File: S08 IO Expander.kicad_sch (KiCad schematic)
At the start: 13 parts, among them Q23 BSS138, U11 PCAL9714

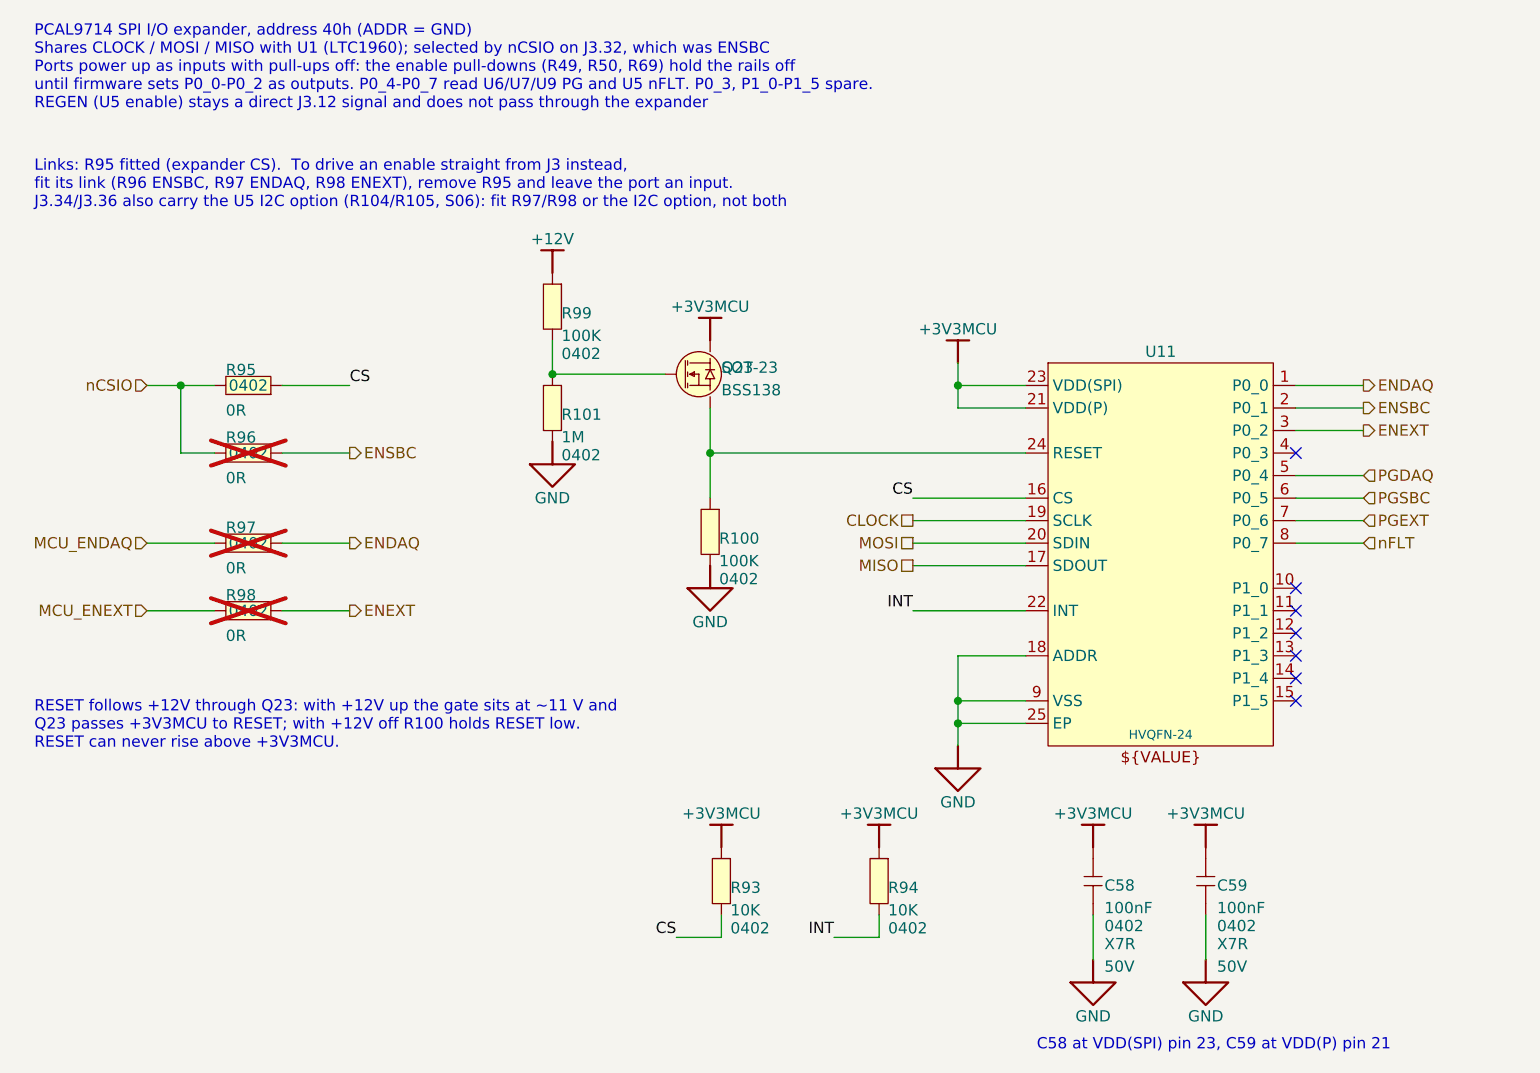
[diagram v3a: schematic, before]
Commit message: Final-revision value changes and standard R/C symbols
Values (schematic and PCB):
- C2 100uF -> 82uF, matching the ordered 35SVPF82M
- C46, C47, C51 (TPS22811 DVDT) 4.7nF -> 1.8nF CC0402KRX7R9BB182 for a
  shorter output ramp
- R24-R27 10R -> 0R; D9, D10 and R36 DNP
- R14 0.01R -> 0.012R PA2512FKF7W0R012E

Symbols:
- All 160 resistors and capacitors now use Device:R, Device:C and
  Device:C_Polarized; the 76 per-value R/C symbols are removed from the
  project library. Connectivity is unchanged (netlist compared).
- Value is now the displayed field instead of ALTIUM_VALUE, which had left
  R1, C39 and R54 showing their old values. ALTIUM_VALUE synced with Value
  on R1, C39, R54, D1, Q1, Q3 and L1.
- Net-(C40-+) is now Net-(U5-ISNSP); renamed on the PCB and in the
  PWR 15A net class pattern.

Co-Authored-By: Claude Opus 5.5 <noreply@anthropic.com>
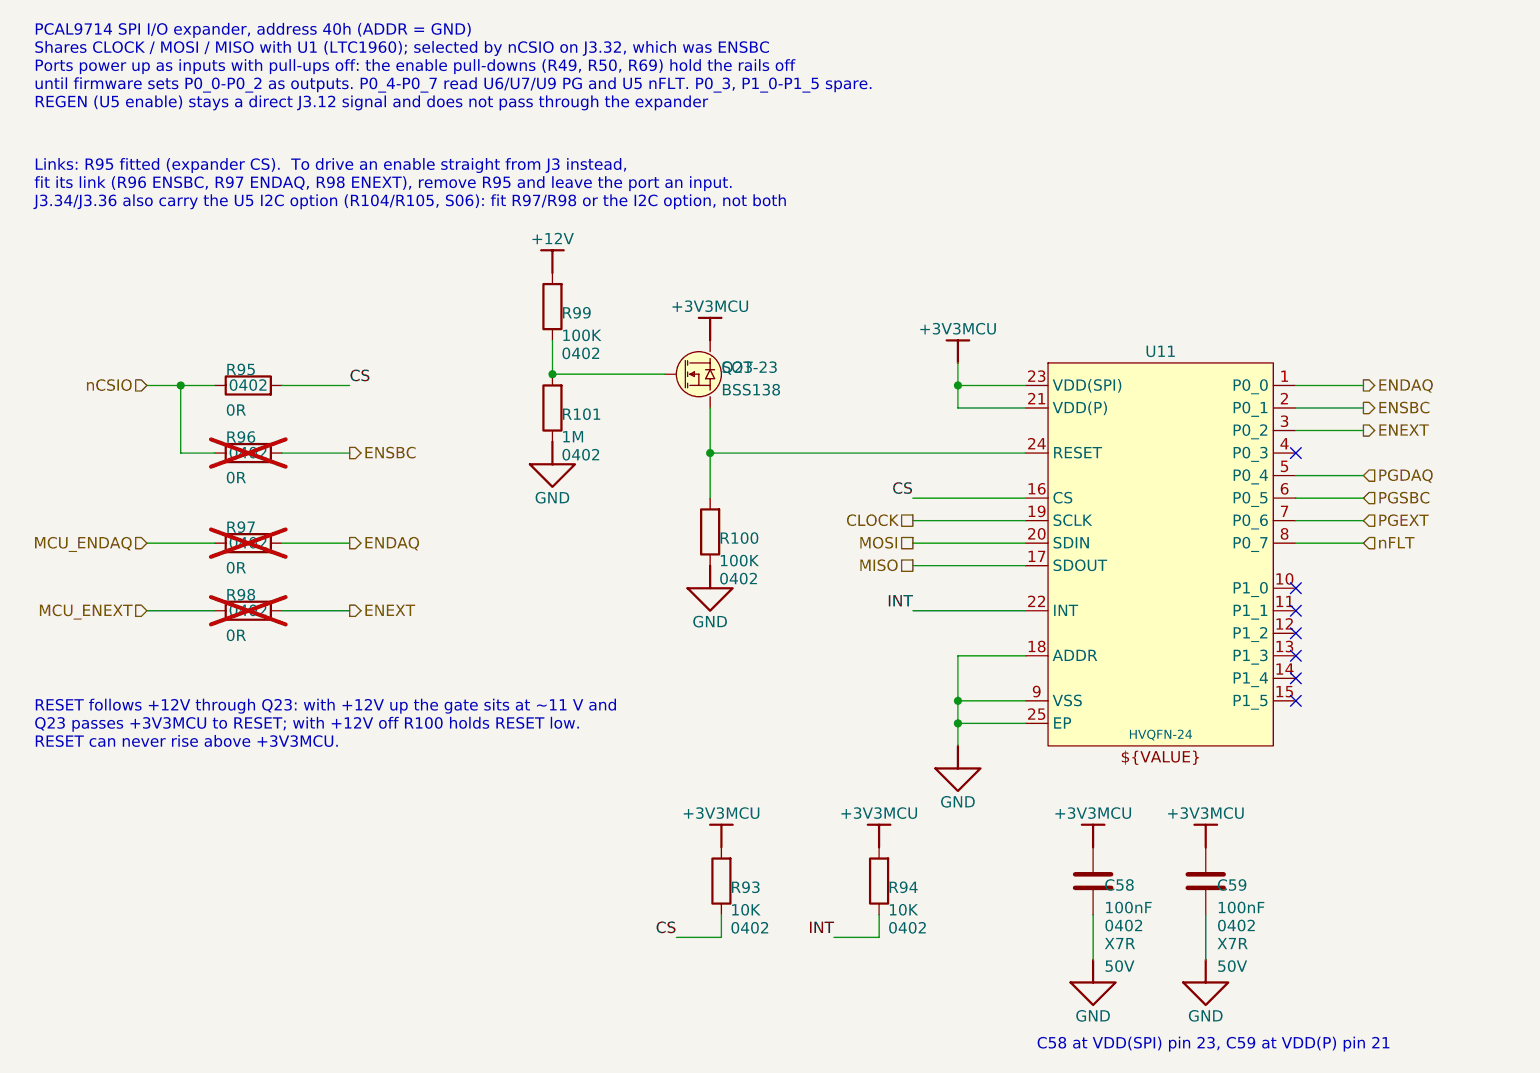
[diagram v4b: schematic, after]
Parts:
- C58, C59: symbol Lattech Systems:Capacitor 100nF 50V X7R 0402 -> Device:C
- R100, R99: symbol Lattech Systems:Resistor 100K 1% 0402 -> Device:R
- R101: symbol Lattech Systems:Resistor 1M 1% 0402 -> Device:R
- R93, R94: symbol Lattech Systems:Resistor 10K 1% 0402 -> Device:R
- R95, R96, R97, R98: symbol Lattech Systems:Resistor 0R 0402 -> Device:R

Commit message: Retune load-switch OVLO and PG dividers; add design constraint notes
- R90-R92 1M -> 1.07M: OVLO trips at 14.0 V (13.40-14.69 V) and recovers
  below 12.75 V (at least 12.23 V), so a tripped switch always comes back
  on the 12.03 V rail. R101 (Q23 gate divider) -> 1.07M to share the line.
- PGTH dividers R59/R61/R76 1M -> 100K and R60/R62/R77 130K -> 13K: same
  10.43 V threshold, but the +-1 uA pin leakage now moves it 0.1 V, not
  1 V; worst-case rising 10.93 V instead of 11.84 V.
- Schematic notes for the W16 constraints: J2 contacts (S01), R16 latching
  breaker and ED29/QE29 trip currents (S03), R19 vs L1 saturation (S04),
  R22 presence pull-up (S05), R42 and the U5 MODE/ILIMCOMP/VCC2 pins (S06),
  and the OVLO/PG divider settings (S07).
- README: OVLO and PG divider figures, and the EN_CONST_TDEAD default for
  the I2C build.

Co-Authored-By: Claude Opus 5.5 <noreply@anthropic.com>
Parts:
- R101: value 1M -> 1.07M; ALTIUM_VALUE 1M -> 1.07M
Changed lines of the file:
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@@
 			)
 		)
-		(property "Value" "1M"
+		(property "Value" "1.07M"
 			(at 122.936 111.76 0)
 			(show_name no)
@@
 			)
 		)
-		(property "Description" "Resistor 1M 1% 0402"
+		(property "Description" "Resistor 1.07M 1% 0402"
 			(at 121.92 109.22 90)
 			(hide yes)
@@
 			)
 		)
-		(property "ALTIUM_VALUE" "1M"
+		(property "ALTIUM_VALUE" "1.07M"
 			(at 120.904 104.902 0)
 			(hide yes)

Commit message: Add an 11 V undervoltage lockout to the DAQ load switch
- R108 100K from +12V over R49 (100K -> 12K) on U6 EN/UVLO: on at 11.2 V
  (10.77-11.69 V), off at 10.17 V (9.83-10.66 V). The TPS22811's fixed
  hysteresis makes 11 V the turn-on point.
- Q24 (BSS138) from EN/UVLO to GND takes over the enable. Its gate is biased
  from +12V by R109 100K / R110 27K (2.55 V), so U6 stays in shutdown when
  the expander is in reset, unpowered, or the MCU board is off.
- The expander net ENDAQ is now nENDAQ, active low (S07, S08, root sheet).
  The gate stays under 3.3 V, so P0_0 can stay push-pull and the R97
  fallback can drive it from a 3.3 V MCU pin.
- S07 note marks the DAQ circuit as deliberate; S08 notes and README
  updated.

The PCB still needs Update PCB from Schematic: Q24 and R108-R110 are
missing, R49 has its old value, and /ENDAQ is split into two nets.

Co-Authored-By: Claude Opus 5.5 <noreply@anthropic.com>
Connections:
- net ENDAQ renamed nENDAQ
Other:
- note added: "Links: R95 fitted (expander CS). To drive an enable straight from J3 instead, fit its link (R96 ENSBC, R97 nENDAQ active low, R98 ENEXT), remove R95 and leave the port an input. J3.34/J3.36 also carry the U5 I2C option (R104/R105, S06): fit R97/R98 or the I2C option, not both"
- note added: "PCAL9714 SPI I/O expander, address 40h (ADDR = GND) Shares CLOCK / MOSI / MISO with U1 (LTC1960); selected by nCSIO on J3.32, which was ENSBC Ports power up as inputs with pull-ups off: the enable pull-downs (R50, R69) and Q24's gate bias (DAQ) hold the rails off until firmware sets P0_0-P0_2 as outputs. P0_0 (nENDAQ) is active LOW. P0_4-P0_7 read U6/U7/U9 PG and U5 nFLT. P0_3, P1_0-P1_5 spare. R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"
- note removed: "Links: R95 fitted (expander CS). To drive an enable straight from J3 instead, fit its link (R96 ENSBC, R97 ENDAQ, R98 ENEXT), remove R95 and leave the port an input. J3.34/J3.36 also carry the U5 I2C option (R104/R105, S06): fit R97/R98 or the I2C option, not both"
- note removed: "PCAL9714 SPI I/O expander, address 40h (ADDR = GND) Shares CLOCK / MOSI / MISO with U1 (LTC1960); selected by nCSIO on J3.32, which was ENSBC Ports power up as inputs with pull-ups off: the enable pull-downs (R49, R50, R69) hold the rails off until firmware sets P0_0-P0_2 as outputs. P0_4-P0_7 read U6/U7/U9 PG and U5 nFLT. P0_3, P1_0-P1_5 spare. REGEN (U5 enable) stays a direct J3.12 signal and d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"
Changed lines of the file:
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@@
 	(generator_version "10.0")
 	(paper "A3")
-	(text "Links: R95 fitted (expander CS).  To drive an enable straight from J3 instead,\nfit its link (R96 ENSBC, R97 ENDAQ, R98 ENEXT), remove R95 and leave the port an input.\nJ3.34/J3.36 also carry the U5 I2C option (R104/R105, S06): fit R97/R98 or the I2C option, not both"
+	(text "Links: R95 fitted (expander CS).  To drive an enable straight from J3 instead,\nfit its link (R96 ENSBC, R97 nENDAQ active low, R98 ENEXT), remove R95 and leave the port an input.\nJ3.34/J3.36 also carry the U5 I2C option (R104/R105, S06): fit R97/R98 or the I2C option, not both"
 		(exclude_from_sim no)
 		(at 63.5 81.28 0)
@@
 		)
 	)
-	(text "PCAL9714 SPI I/O expander, address 40h (ADDR = GND)\nShares CLOCK / MOSI / MISO with U1 (LTC1960); selected by nCSIO on J3.32, which was ENSBC\nPorts power up as inputs with pull-ups off: the enable pull-downs (R49, R50, R69) hold the rails off\nuntil firmware sets P0_0-P0_2 as outputs. P0_4-P0_7 read U6/U7/U9 PG and U5 nFLT. P0_3, P1_0-P1_5 spare.\nREGEN (U5 enable) stays a direct J3.12 signal and does not pass through the expander"
+	(text "PCAL9714 SPI I/O expander, address 40h (ADDR = GND)\nShares CLOCK / MOSI / MISO with U1 (LTC1960); selected by nCSIO on J3.32, which was ENSBC\nPorts power up as inputs with pull-ups off: the enable pull-downs (R50, R69) and Q24's gate bias (DAQ) hold the rails off\nuntil firmware sets P0_0-P0_2 as outputs. P0_0 (nENDAQ) is active LOW. P0_4-P0_7 read U6/U7/U9 PG and U5 nFLT. P0_3, P1_0-P1_5 spare.\nREGEN (U5 enable) stays a direct J3.12 signal and does not pass through the expander"
 		(exclude_from_sim no)
 		(at 63.5 66.04 0)
@@
 		)
 	)
-	(hierarchical_label "ENDAQ"
+	(hierarchical_label "nENDAQ"
 		(shape output)
 		(at 99.06 124.46 0)
@@
 		)
 	)
-	(hierarchical_label "ENDAQ"
+	(hierarchical_label "nENDAQ"
 		(shape output)
 		(at 213.36 106.68 0)

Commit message: PCB routing and DRC clean-up; teardrops; title block to 0.6.0
PCB (manual edits in KiCad):
- Route more of the new parts: +59 track segments, +7 vias, and a small
  +3V3MCU pour on In6.Cu near J3 (x 159, y 130-134).
- Add teardrops (319). Teardrop and zone defaults updated in the
  project settings.
- DRC with schematic parity: 285 -> 98 violations (64 padstack,
  27 unrouted pads, 19 + 2 silk, 8 text thickness, 5 dangling vias).
  No parity, clearance, short or courtyard errors.

Project: title-block variables BOARD_NUMBER EVO2513-0.6.0 and
COMP_NAME evoSonic; extra track width (0.15/0.5 mm) presets.

Schematics: cosmetic only (field positions, element order, S03 FET
pin entries). No value, footprint, DNP, net or note changes.

Molex 105310xx04 footprint: courtyard rectangle redrawn.

Co-Authored-By: Claude Opus 5.5 <noreply@anthropic.com>
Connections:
- net ENSBC: now also U11.1 (P0_0); no longer U11.2 (P0_1)
- net nENDAQ: now also U11.2 (P0_1); no longer U11.1 (P0_0)
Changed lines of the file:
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@@
+	(wire
+		(pts
+			(xy 205.74 111.76) (xy 213.36 111.76)
+		)
+		(stroke
+			(width 0)
+			(type default)
+		)
+	)
+	(wire
+		(pts
+			(xy 140.97 168.91) (xy 135.89 168.91)
+		)
+		(stroke
+			(width 0)
+			(type default)
+		)
+	)
+	(wire
+		(pts
+			(xy 205.74 119.38) (xy 213.36 119.38)
+		)
+		(stroke
+			(width 0)
+			(type default)
+		)
+	)
+	(wire
+		(pts
+			(xy 195.58 166.37) (xy 195.58 171.45)
+		)
+		(stroke
+			(width 0)
+			(type default)
+		)
+	)
+	(wire
+		(pts
+			(xy 76.2 124.46) (xy 83.82 124.46)
+		)
+		(stroke
+			(width 0)
+			(type default)
+		)
+	)
+	(wire
+		(pts
+			(xy 175.26 127) (xy 162.56 127)
+		)
+		(stroke
+			(width 0)
+			(type default)
+		)
+	)
+	(wire
+		(pts
+			(xy 91.44 132.08) (xy 99.06 132.08)
+		)
+		(stroke
+			(width 0)
+			(type default)
+		)
+	)
+	(wire
+		(pts
+			(xy 167.64 104.14) (xy 167.64 109.22)
+		)
+		(stroke
+			(width 0)
+			(type default)
+		)
+	)
+	(wire
+		(pts
+			(xy 91.44 124.46) (xy 99.06 124.46)
+		)
+		(stroke
+			(width 0)
+			(type default)
+		)
+	)
+	(wire
+		(pts
+			(xy 80.01 106.68) (xy 80.01 114.3)
+		)
+		(stroke
+			(width 0)
+			(type default)
+		)
+	)
+	(wire
+		(pts
+			(xy 205.74 109.22) (xy 213.36 109.22)
+		)
+		(stroke
+			(width 0)
+			(type default)
+		)
+	)
+	(wire
+		(pts
+			(xy 140.97 166.37) (xy 140.97 168.91)
+		)
+		(stroke
+			(width 0)
+			(type default)
+		)
+	)
+	(wire
+		(pts
+			(xy 182.88 166.37) (xy 182.88 171.45)
+		)
+		(stroke
+			(width 0)
+			(type default)
+		)
+	)
+	(wire
+		(pts
+			(xy 121.92 101.6) (xy 121.92 105.41)
+		)
+		(stroke
+			(width 0)
+			(type default)
+		)
+	)
+	(wire
+		(pts
+			(xy 139.7 109.22) (xy 139.7 119.38)
+		)
+		(stroke
+			(width 0)
+			(type default)
+		)
+	)
+	(wire
+		(pts
+			(xy 175.26 109.22) (xy 167.64 109.22)
+		)
+		(stroke
+			(width 0)
+			(type default)
+		)
+	)
+	(wire
+		(pts
+			(xy 121.92 105.41) (xy 134.62 105.41)
+		)
+		(stroke
+			(width 0)
+			(type default)
+		)
+	)
+	(wire
+		(pts
+			(xy 205.74 124.46) (xy 213.36 124.46)
+		)
+		(stroke
+			(width 0)
+			(type default)
+		)
+	)
+	(wire
+		(pts
+			(xy 91.44 114.3) (xy 99.06 114.3)
+		)
+		(stroke
+			(width 0)
+			(type default)
+		)
+	)
 	(wire
 		(pts
 			(xy 205.74 106.68) (xy 213.36 106.68)
-		)
-		(stroke
-			(width 0)
-			(type default)
-		)
-	)
-	(wire
-		(pts
-			(xy 205.74 111.76) (xy 213.36 111.76)
-		)
-		(stroke
-			(width 0)
-			(type default)
-		)
-	)
-	(wire
-		(pts
-			(xy 140.97 168.91) (xy 135.89 168.91)
-		)
-		(stroke
-			(width 0)
-			(type default)
-		)
-	)
-	(wire
-		(pts
-			(xy 205.74 119.38) (xy 213.36 119.38)
-		)
-		(stroke
-			(width 0)
-			(type default)
-		)
-	)
-	(wire
-		(pts
-			(xy 195.58 166.37) (xy 195.58 171.45)
-		)
-		(stroke
-			(width 0)
-			(type default)
-		)
-	)
-	(wire
-		(pts
-			(xy 76.2 124.46) (xy 83.82 124.46)
-		)
-		(stroke
-			(width 0)
-			(type default)
-		)
-	)
-	(wire
-		(pts
-			(xy 175.26 127) (xy 162.56 127)
-		)
-		(stroke
-			(width 0)
-			(type default)
-		)
-	)
-	(wire
-		(pts
-			(xy 205.74 109.22) (xy 213.36 109.22)
-		)
-		(stroke
-			(width 0)
-			(type default)
-		)
-	)
-	(wire
-		(pts
-			(xy 91.44 132.08) (xy 99.06 132.08)
-		)
-		(stroke
-			(width 0)
-			(type default)
-		)
-	)
-	(wire
-		(pts
-			(xy 167.64 104.14) (xy 167.64 109.22)
-		)
-		(stroke
-			(width 0)
-			(type default)
-		)
-	)
-	(wire
-		(pts
-			(xy 91.44 124.46) (xy 99.06 124.46)
-		)
-		(stroke
-			(width 0)
-			(type default)
-		)
-	)
-	(wire
-		(pts
-			(xy 80.01 106.68) (xy 80.01 114.3)
-		)
-		(stroke
-			(width 0)
-			(type default)
-		)
-	)
-	(wire
-		(pts
-			(xy 140.97 166.37) (xy 140.97 168.91)
-		)
-		(stroke
-			(width 0)
-			(type default)
-		)
-	)
-	(wire
-		(pts
-			(xy 182.88 166.37) (xy 182.88 171.45)
-		)
-		(stroke
-			(width 0)
-			(type default)
-		)
-	)
-	(wire
-		(pts
-			(xy 121.92 101.6) (xy 121.92 105.41)
-		)
-		(stroke
-			(width 0)
-			(type default)
-		)
-	)
-	(wire
-		(pts
-			(xy 139.7 109.22) (xy 139.7 119.38)
-		)
-		(stroke
-			(width 0)
-			(type default)
-		)
-	)
-	(wire
-		(pts
-			(xy 175.26 109.22) (xy 167.64 109.22)
-		)
-		(stroke
-			(width 0)
-			(type default)
-		)
-	)
-	(wire
-		(pts
-			(xy 121.92 105.41) (xy 134.62 105.41)
-		)
-		(stroke
-			(width 0)
-			(type default)
-		)
-	)
-	(wire
-		(pts
-			(xy 205.74 124.46) (xy 213.36 124.46)
-		)
-		(stroke
-			(width 0)
-			(type default)
-		)
-	)
-	(wire
-		(pts
-			(xy 91.44 114.3) (xy 99.06 114.3)
 		)
 		(stroke
@@
 	(hierarchical_label "nENDAQ"
 		(shape output)
-		(at 213.36 106.68 0)
+		(at 213.36 109.22 0)
 		(effects
 			(font
@@
 	(hierarchical_label "ENSBC"
 		(shape output)
-		(at 213.36 109.22 0)
-		(effects
-			(font
+		(at 213.36 106.68 0)
+		(effects
+			(font

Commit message: U11 PCAL9714HNMP 3D model; FET zone reshaping; R23/R82-R85 DNP
- U11 moves to a project-library copy of HVQFN-24-1EP_4x4mm_P0.5mm_EP2.6x2.6mm
  linked to ${KIPRJMOD}/PCAL9714HNMP.stp (STEP later embedded; file not kept). Schematic and Lattech
  symbol point at the project copy.
- Board updated from the schematic (symbol pin data on the swapped
  footprints) and zone fills reshaped around the FETs.
- R23, R82-R85 (NEQ) set DNP in the schematic and on the board.

DRC: 0 errors, 0 unconnected, 0 schematic parity issues. ERC: 0 violations.

Co-Authored-By: Claude Opus 5.5 <noreply@anthropic.com>
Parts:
- U11: footprint Package_DFN_QFN:HVQFN-24-1EP_4x4mm_P0.5mm_EP2.6x2.6mm -> EVO2513-0_5_0-import-fps:HVQFN-24-1EP_4x4mm_P0.5mm_EP2.6x2.6mm
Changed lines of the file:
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@@
 			)
 		)
-		(property "Footprint" "Package_DFN_QFN:HVQFN-24-1EP_4x4mm_P0.5mm_EP2.6x2.6mm"
+		(property "Footprint" "EVO2513-0_5_0-import-fps:HVQFN-24-1EP_4x4mm_P0.5mm_EP2.6x2.6mm"
 			(at 190.5 119.38 0)
 			(hide yes)
